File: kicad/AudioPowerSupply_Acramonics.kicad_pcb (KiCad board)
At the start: 2 copper layers, 95.8 x 71.3 mm, 41 parts, among them J2 Conn_01x04_Pin, J5 48V out, U1 LM7815_TO220, U2 LM7915_TO220, U3 LM317_TO-220

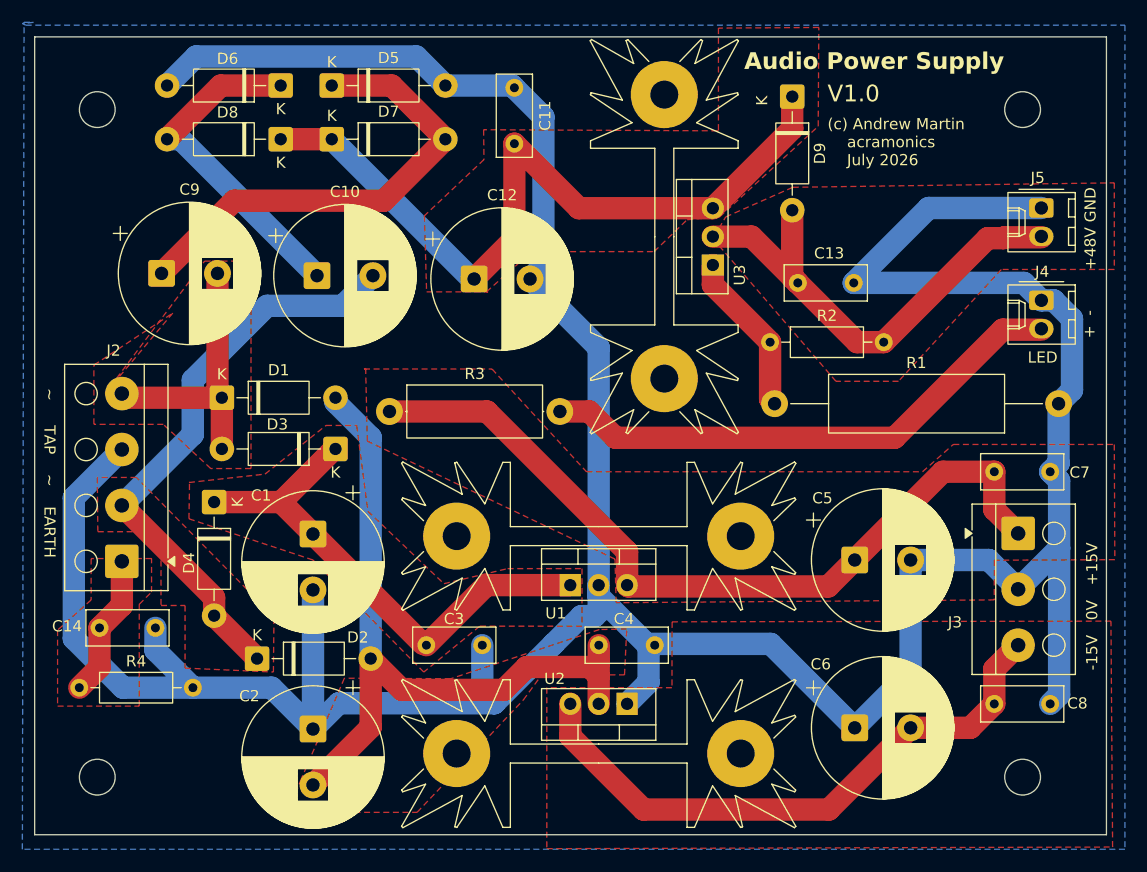
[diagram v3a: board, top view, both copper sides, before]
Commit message: Added line to divide 48V section
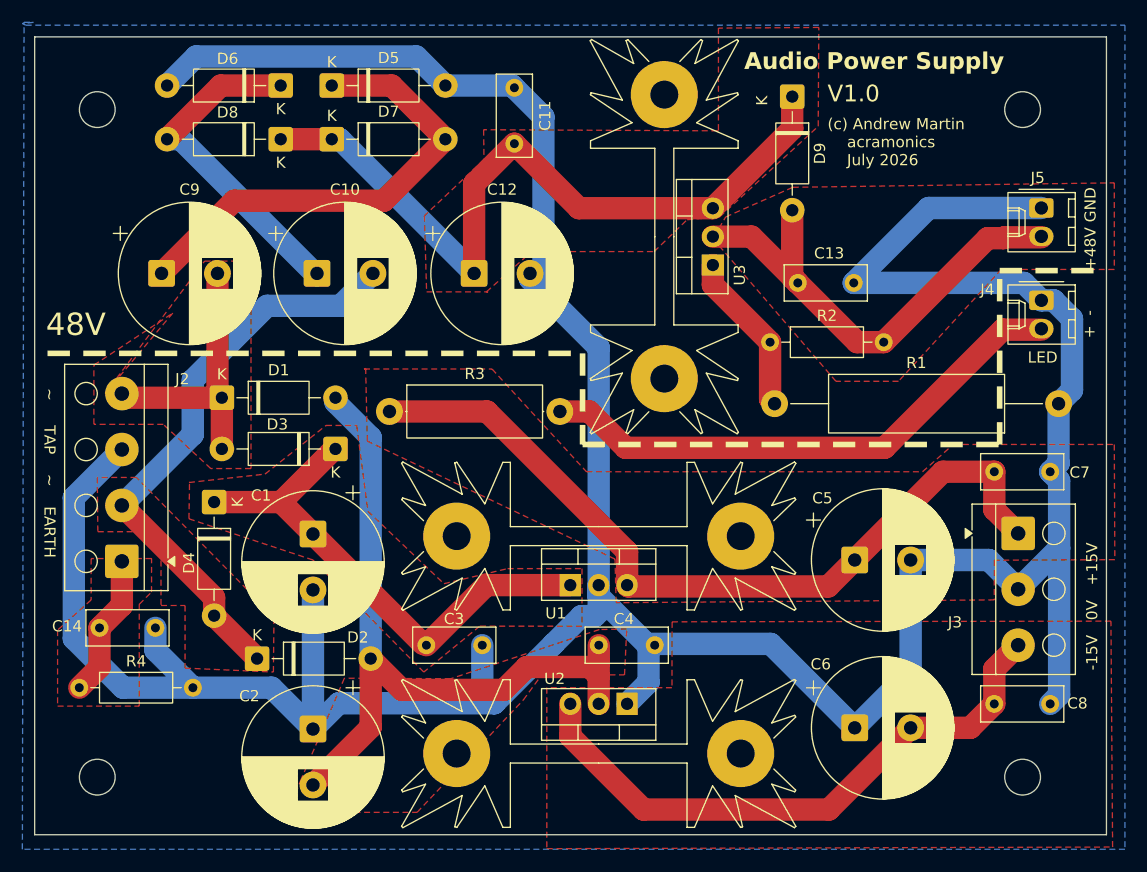
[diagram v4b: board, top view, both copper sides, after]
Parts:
- moved C12 0.50 mm to (96.7, 88.7)
- moved C10 0.20 mm to (82.7, 88.7)
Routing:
- net Net-(J4-Pin_2): track 48.0 -> 48.8 mm
- net Net-(D7-K): track 69.1 -> 68.4 mm
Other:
- board text added: "48V"
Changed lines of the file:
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@@
 		(tags "THT Terminal block Altech AK100 pitch 5mm size 20x9mm drill 1.3mm pad 3mm")
 		(property "Reference" "J2"
-			(at 18.85 -0.75 0)
+			(at 16.3 5.4 0)
 			(layer "F.SilkS")
 			(effects
@@
 	(footprint "Capacitor_THT:CP_Radial_D12.5mm_P5.00mm"
 		(layer "F.Cu")
-		(at 96.7 89.15)
+		(at 96.7 88.65)
 		(descr "CP, Radial series, Radial, pin pitch=5.00mm, diameter=12.5mm, height=20mm, Electrolytic Capacitor")
 		(tags "CP Radial series Radial pin pitch 5.00mm diameter 12.5mm height 20mm Electrolytic Capacitor")
@@
 	(footprint "Capacitor_THT:CP_Radial_D12.5mm_P5.00mm"
 		(layer "F.Cu")
-		(at 82.65 88.85)
+		(at 82.65 88.65)
 		(descr "CP, Radial series, Radial, pin pitch=5.00mm, diameter=12.5mm, height=20mm, Electrolytic Capacitor")
 		(tags "CP Radial series Radial pin pitch 5.00mm diameter 12.5mm height 20mm Electrolytic Capacitor")
@@
 		(tags "connector Molex KK-254 vertical")
 		(property "Reference" "J4"
-			(at -2.56 -0.07 0)
+			(at -0.96 4.83 0)
 			(layer "F.SilkS")
 			(effects
@@
 		)
 	)
+	(gr_line
+		(start 58.55 95.8)
+		(end 106.4 95.8)
+		(stroke
+			(width 0.5)
+			(type dash_dot)
+		)
+		(layer "F.SilkS")
+	)
+	(gr_line
+		(start 106.4 95.8)
+		(end 106.4 103.95)
+		(stroke
+			(width 0.5)
+			(type dash_dot)
+		)
+		(layer "F.SilkS")
+	)
+	(gr_line
+		(start 106.4 103.95)
+		(end 143.7 103.95)
+		(stroke
+			(width 0.5)
+			(type dash_dot)
+		)
+		(layer "F.SilkS")
+	)
+	(gr_line
+		(start 143.7 88.4)
+		(end 153.25 88.4)
+		(stroke
+			(width 0.5)
+			(type dash_dot)
+		)
+		(layer "F.SilkS")
+	)
+	(gr_line
+		(start 143.7 103.95)
+		(end 143.7 88.4)
+		(stroke
+			(width 0.5)
+			(type dash_dot)
+		)
+		(layer "F.SilkS")
+	)
 	(gr_rect
 		(start 57.4 67.5)
@@
 		)
 	)
+	(gr_text "48V"
+		(at 58.4 94.4 0)
+		(layer "F.SilkS")
+		(effects
+			(font
+				(size 2 2)
+				(thickness 0.25)
+			)
+			(justify left bottom)
+		)
+	)
 	(segment
 		(start 79.4 71.85)
@@
 	)
 	(segment
-		(start 78.178198 91.55)
-		(end 84.95 91.55)
+		(start 84.75 91.55)
+		(end 87.65 88.65)
 		(width 2)
 		(layer "B.Cu")
@@
 	)
 	(segment
-		(start 71.54 103.06)
-		(end 71.54 98.188198)
+		(start 78.178198 91.55)
+		(end 84.75 91.55)
 		(width 2)
 		(layer "B.Cu")
@@
 	)
 	(segment
-		(start 71.54 98.188198)
-		(end 78.178198 91.55)
+		(start 71.54 103.06)
+		(end 71.54 98.188198)
 		(width 2)
 		(layer "B.Cu")
@@
 	)
 	(segment
-		(start 84.95 91.55)
-		(end 87.65 88.85)
+		(start 71.54 98.188198)
+		(end 78.178198 91.55)
 		(width 2)
 		(layer "B.Cu")
@@
 	)
 	(segment
-		(start 125.15 75.72)
-		(end 118.05 82.82)
+		(start 96.7 80.65)
+		(end 100.3 77.05)
 		(width 2)
 		(layer "F.Cu")
@@
 	)
 	(segment
-		(start 100.3 77.05)
-		(end 100.3 85.55)
+		(start 96.7 88.65)
+		(end 96.7 80.65)
 		(width 2)
 		(layer "F.Cu")
@@
 	)
 	(segment
-		(start 125.15 72.84)
-		(end 125.15 75.72)
+		(start 125.15 75.72)
+		(end 118.05 82.82)
 		(width 2)
 		(layer "F.Cu")
@@
 	)
 	(segment
-		(start 96.7 89.15)
-		(end 96.47 89.15)
+		(start 125.15 72.84)
+		(end 125.15 75.72)
 		(width 2)
 		(layer "F.Cu")
@@
 	)
 	(segment
-		(start 100.3 85.55)
-		(end 96.7 89.15)
+		(start 118.05 82.82)
+		(end 106.07 82.82)
 		(width 2)
 		(layer "F.Cu")
@@
 	)
 	(segment
-		(start 118.05 82.82)
-		(end 106.07 82.82)
+		(start 83.97 76.65)
+		(end 84.7 76.65)
 		(width 2)
-		(layer "F.Cu")
+		(layer "B.Cu")
 		(net "Net-(D7-K)")
 	)
 	(segment
-		(start 96.47 89.15)
-		(end 83.97 76.65)
+		(start 84.7 76.65)
+		(end 96.7 88.65)
 		(width 2)
 		(layer "B.Cu")
@@
 	)
 	(segment
-		(start 107 101)
-		(end 109.35 103.35)
+		(start 110.25 104.25)
+		(end 133.4 104.25)
 		(width 2)
 		(layer "F.Cu")
@@
 	)
 	(segment
-		(start 104.37 101)
-		(end 107 101)
+		(start 107 101)
+		(end 110.25 104.25)
 		(width 2)
 		(layer "F.Cu")
@@
 	)
 	(segment
-		(start 134.3 103.35)
-		(end 143.97 93.68)
+		(start 104.37 101)
+		(end 107 101)
 		(width 2)
 		(layer "F.Cu")
@@
 	)
 	(segment
-		(start 109.35 103.35)
-		(end 134.3 103.35)
+		(start 133.4 104.25)
+		(end 143.97 93.68)
 		(width 2)
 		(layer "F.Cu")
